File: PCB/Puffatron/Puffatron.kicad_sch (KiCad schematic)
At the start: 10 parts, among them U1 RP2040-ZERO, U10 ULN2803A, U2 MCP23017_SP, U3 ULN2803A, U4 MCP23017_SP, U5 MCP23017_SP, U6 ULN2803A, U7 ULN2803A, U8 ULN2803A, U9 ULN2803A

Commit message: README
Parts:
- added Brd1: SSD1306, symbol SSD1306-128x64_OLED:SSD1306
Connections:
- net GNDREF: now also Brd1.1 (GND)
- net at U1.10 (GP9): now also U1.4 (GP3), U1.5 (GP4), U1.6 (GP5), U1.7 (GP6), U1.8 (GP7), U1.9 (GP8), Brd1.3 (SCL)
- net at U1.23 (5V), U2.9 (VDD), U4.16 (A1)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: now also Brd1.2 (VCC)
- net at U1.3 (GP2): now also Brd1.4 (SDA)
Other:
- note added: "OLED"
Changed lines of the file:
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@@
     (date "2026-08-04")
   )
+  (junction (at 67.31 90.17) (diameter 0) (color 0 0 0 0)
+  )
   (junction (at 67.31 125.73) (diameter 0) (color 0 0 0 0)
   )
@@
   (junction (at 85.09 63.5) (diameter 0) (color 0 0 0 0)
   )
+  (junction (at 24.13 58.42) (diameter 0) (color 0 0 0 0)
+  )
   (junction (at 67.31 35.56) (diameter 0) (color 0 0 0 0)
   )
@@
   (junction (at 102.87 191.77) (diameter 0) (color 0 0 0 0)
   )
+  (junction (at 24.13 53.34) (diameter 0) (color 0 0 0 0)
+  )
   (junction (at 76.2 25.4) (diameter 0) (color 0 0 0 0)
   )
+  (junction (at 24.13 63.5) (diameter 0) (color 0 0 0 0)
+  )
   (junction (at 175.26 140.97) (diameter 0) (color 0 0 0 0)
   )
   (junction (at 175.26 82.55) (diameter 0) (color 0 0 0 0)
   )
+  (junction (at 24.13 66.04) (diameter 0) (color 0 0 0 0)
+  )
   (junction (at 175.26 99.06) (diameter 0) (color 0 0 0 0)
   )
   (junction (at 82.55 22.86) (diameter 0) (color 0 0 0 0)
   )
+  (junction (at 24.13 60.96) (diameter 0) (color 0 0 0 0)
+  )
+  (junction (at 24.13 55.88) (diameter 0) (color 0 0 0 0)
+  )
   (wire (pts (xy 125.73 60.96) (xy 129.54 60.96))
     (stroke (width 0) (type default))
@@
     (stroke (width 0) (type default))
   )
+  (wire (pts (xy 39.37 95.25) (xy 39.37 90.17))
+    (stroke (width 0) (type default))
+  )
+  (wire (pts (xy 24.13 86.36) (xy 41.91 86.36))
+    (stroke (width 0) (type default))
+  )
   (wire (pts (xy 125.73 115.57) (xy 125.73 123.19))
     (stroke (width 0) (type default))
@@
     (stroke (width 0) (type default))
   )
+  (wire (pts (xy 24.13 53.34) (xy 24.13 55.88))
+    (stroke (width 0) (type default))
+  )
   (wire (pts (xy 120.65 58.42) (xy 123.19 58.42))
     (stroke (width 0) (type default))
@@
     (stroke (width 0) (type default))
   )
+  (wire (pts (xy 24.13 58.42) (xy 24.13 60.96))
+    (stroke (width 0) (type default))
+  )
   (wire (pts (xy 24.13 16.51) (xy 82.55 16.51))
     (stroke (width 0) (type default))
   )
+  (wire (pts (xy 44.45 81.28) (xy 44.45 95.25))
+    (stroke (width 0) (type default))
+  )
   (wire (pts (xy 168.91 140.97) (xy 175.26 140.97))
     (stroke (width 0) (type default))
@@
     (stroke (width 0) (type default))
   )
+  (wire (pts (xy 24.13 66.04) (xy 24.13 86.36))
+    (stroke (width 0) (type default))
+  )
   (wire (pts (xy 120.65 113.03) (xy 127 113.03))
     (stroke (width 0) (type default))
@@
     (stroke (width 0) (type default))
   )
+  (wire (pts (xy 41.91 86.36) (xy 41.91 95.25))
+    (stroke (width 0) (type default))
+  )
+  (wire (pts (xy 24.13 55.88) (xy 24.13 58.42))
+    (stroke (width 0) (type default))
+  )
   (wire (pts (xy 128.27 118.11) (xy 129.54 118.11))
     (stroke (width 0) (type default))
@@
     (stroke (width 0) (type default))
   )
+  (wire (pts (xy 24.13 60.96) (xy 24.13 63.5))
+    (stroke (width 0) (type default))
+  )
   (wire (pts (xy 128.27 175.26) (xy 129.54 175.26))
     (stroke (width 0) (type default))
@@
     (stroke (width 0) (type default))
   )
+  (wire (pts (xy 19.05 81.28) (xy 44.45 81.28))
+    (stroke (width 0) (type default))
+  )
   (wire (pts (xy 127 58.42) (xy 129.54 58.42))
     (stroke (width 0) (type default))
   )
+  (wire (pts (xy 36.83 95.25) (xy 22.86 95.25))
+    (stroke (width 0) (type default))
+  )
   (wire (pts (xy 120.65 40.64) (xy 148.59 40.64))
     (stroke (width 0) (type default))
   )
+  (wire (pts (xy 22.86 95.25) (xy 22.86 99.06))
+    (stroke (width 0) (type default))
+  )
+  (wire (pts (xy 24.13 63.5) (xy 24.13 66.04))
+    (stroke (width 0) (type default))
+  )
+  (wire (pts (xy 24.13 48.26) (xy 19.05 48.26))
+    (stroke (width 0) (type default))
+  )
+  (wire (pts (xy 67.31 90.17) (xy 67.31 125.73))
+    (stroke (width 0) (type default))
+  )
   (wire (pts (xy 148.59 161.29) (xy 120.65 161.29))
     (stroke (width 0) (type default))
@@
     (stroke (width 0) (type default))
   )
+  (wire (pts (xy 24.13 50.8) (xy 24.13 53.34))
+    (stroke (width 0) (type default))
+  )
   (wire (pts (xy 127 50.8) (xy 127 58.42))
     (stroke (width 0) (type default))
@@
     (stroke (width 0) (type default))
   )
+  (wire (pts (xy 39.37 90.17) (xy 67.31 90.17))
+    (stroke (width 0) (type default))
+  )
   (wire (pts (xy 120.65 184.15) (xy 120.65 190.5))
     (stroke (width 0) (type default))
@@
     (stroke (width 0) (type default))
   )
+  (wire (pts (xy 19.05 48.26) (xy 19.05 81.28))
+    (stroke (width 0) (type default))
+  )
   (wire (pts (xy 125.73 180.34) (xy 129.54 180.34))
     (stroke (width 0) (type default))
@@
     (stroke (width 0) (type default))
   )
-  (wire (pts (xy 67.31 77.47) (xy 67.31 125.73))
+  (wire (pts (xy 67.31 77.47) (xy 67.31 90.17))
     (stroke (width 0) (type default))
   )
@@
   )
   (text "PSU" (at 185.42 92.71 0)
+    (effects (font (size 1.27 1.27)) (justify left bottom))
+  )
+  (text "OLED" (at 38.1 106.68 0)
     (effects (font (size 1.27 1.27)) (justify left bottom))
   )
@@
     )
   )
+  (symbol (lib_id "power:GNDREF") (at 22.86 99.06 0) (unit 1)
+    (in_bom yes) (on_board yes) (dnp no) (fields_autoplaced)
+    (property "Reference" "#PWR010" (at 22.86 105.41 0)
+      (effects (font (size 1.27 1.27)) hide)
+    )
+    (property "Value" "GNDREF" (at 22.86 104.14 0)
+      (effects (font (size 1.27 1.27)))
+    )
+    (property "Footprint" "" (at 22.86 99.06 0)
+      (effects (font (size 1.27 1.27)) hide)
+    )
+    (property "Datasheet" "" (at 22.86 99.06 0)
+      (effects (font (size 1.27 1.27)) hide)
+    )
+    (pin "1")
+    (instances
+      (project "Puffatron"
+        (path "/96bd69bf-07b6-413b-a4db-7565e08c99f5"
+          (reference "#PWR010") (unit 1)
+        )
+      )
+    )
+  )
   (symbol (lib_id "power:GNDREF") (at 59.69 71.12 0) (unit 1)
     (in_bom yes) (on_board yes) (dnp no) (fields_autoplaced)
@@
         )
       )
+    )
+  )
+  (symbol (lib_id "SSD1306-128x64_OLED:SSD1306") (at 40.64 104.14 0) (unit 1)
+    (in_bom yes) (on_board yes) (dnp no) (fields_autoplaced)
+    (property "Reference" "Brd1" (at 48.26 102.87 0)
+      (effects (font (size 1.27 1.27)) (justify left))
+    )
+    (property "Value" "SSD1306" (at 48.26 105.41 0)
+      (effects (font (size 1.27 1.27)) (justify left))
+    )
+    (property "Footprint" "" (at 40.64 97.79 0)
+      (effects (font (size 1.27 1.27)) hide)
+    )
+    (property "Datasheet" "" (at 40.64 97.79 0)
+      (effects (font (size 1.27 1.27)) hide)
+    )
+    (pin "3")
+    (pin "4")
+    (pin "1")
+    (pin "2")
+    (instances
+      (project "Puffatron"
+        (path "/96bd69bf-07b6-413b-a4db-7565e08c99f5"
+          (reference "Brd1") (unit 1)
+        )
+      )

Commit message: Reorg code, update schematic and README
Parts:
- added R1, R2: R_Small, symbol Device:R_Small
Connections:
- net at Brd1.2 (VCC), U2.9 (VDD), U4.16 (A1)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: now also U1.21 (3V3), U2.18 (~{RESET}), U4.18 (~{RESET}), U5.18 (~{RESET}), R1.1, R2.1; no longer U1.23 (5V)
- net at U1.1 (GP0), U2.13 (SDA), U5.13 (SDA): now also U4.13 (SDA), R2.2
- net at U1.2 (GP1), U2.12 (SCK), U5.12 (SCK): now also U4.12 (SCK), R1.2
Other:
- note added: "4k7"

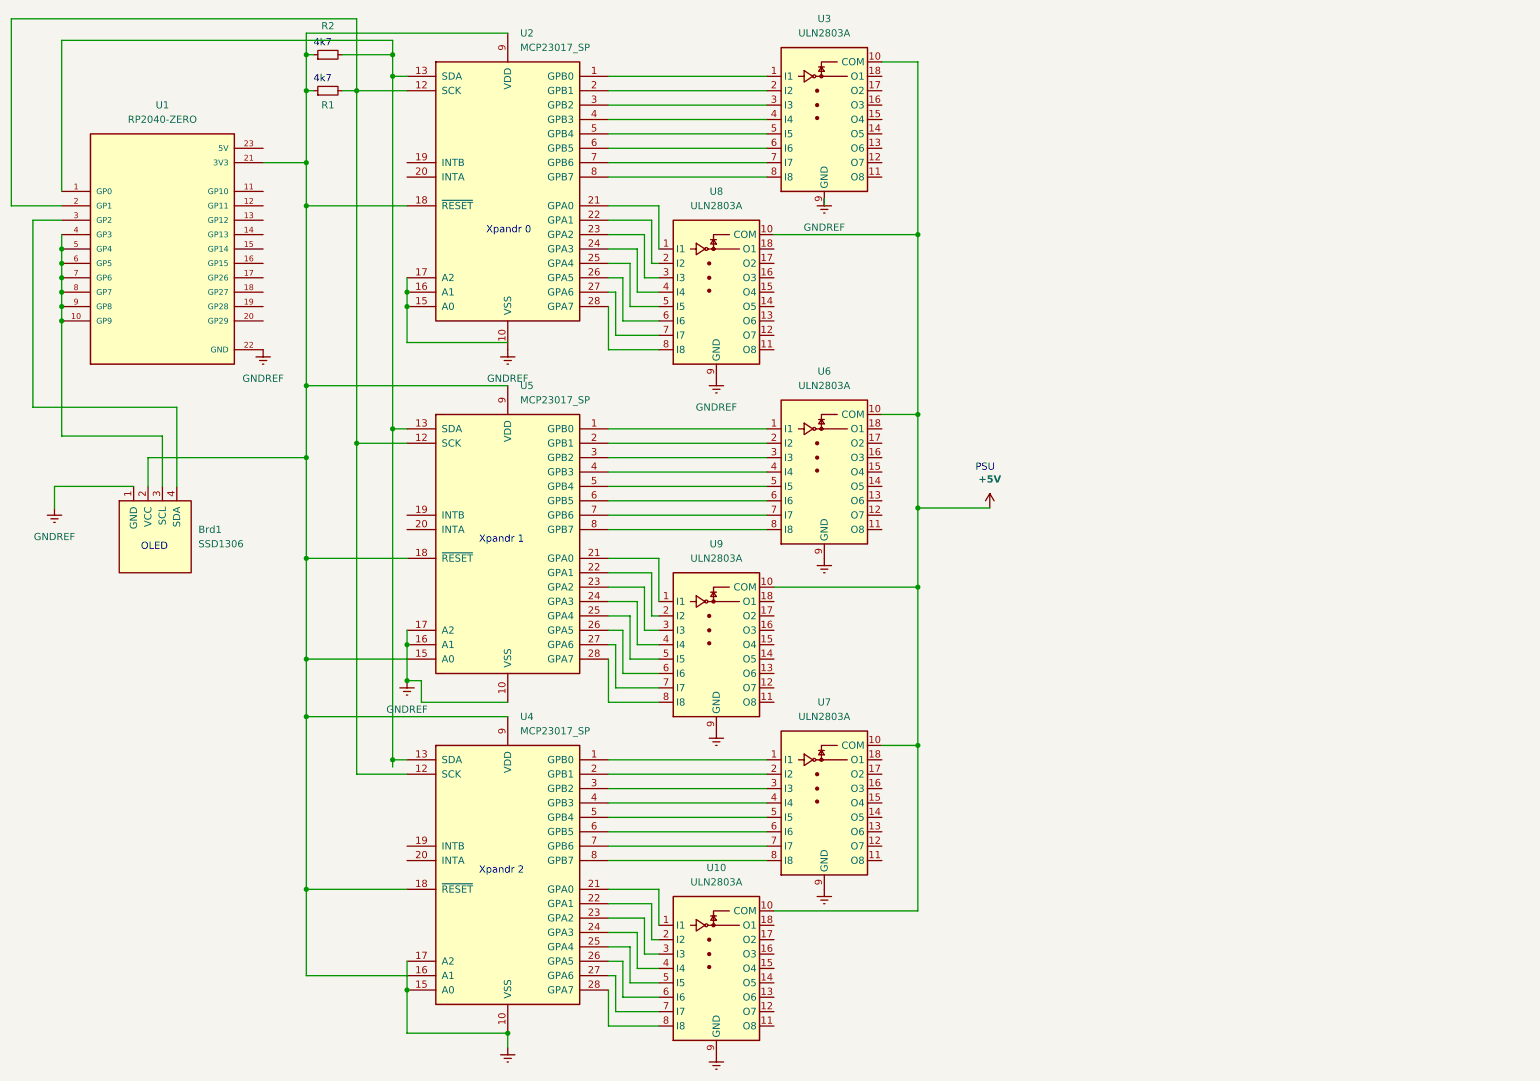
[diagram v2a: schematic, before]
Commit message: Add I2C constants, correct schematic, uptdate docs
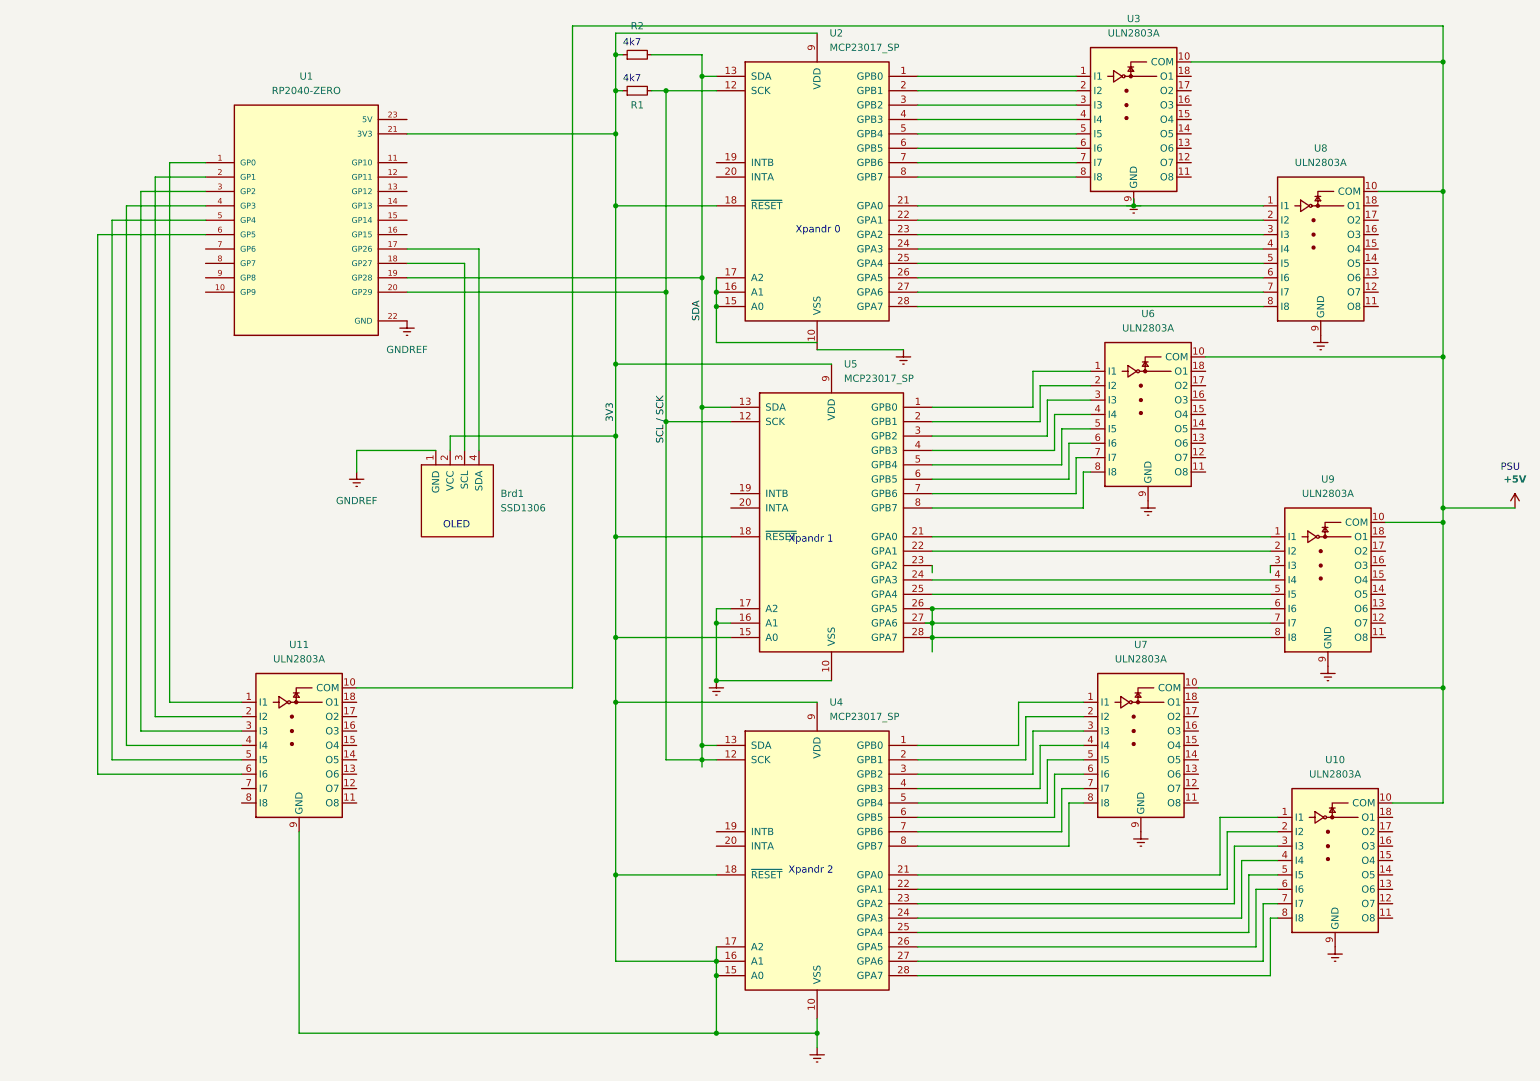
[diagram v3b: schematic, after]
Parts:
- added U11: ULN2803A, symbol Transistor_Array:ULN2803A
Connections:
- net +5V: now also U11.10 (COM)
- net GNDREF: now also Brd1.2 (VCC), R1.1, R2.1, U1.21 (3V3), U2.18 (~{RESET}), U2.21 (GPA0), U2.9 (VDD), U4.16 (A1), U4.18 (~{RESET}), U4.9 (VDD), U5.15 (A0), U5.18 (~{RESET}), U5.9 (VDD), U8.1 (I1), U11.9 (GND)
- net SCL / SCK: now reaches R1.2, U2.12 (SCK), U4.12 (SCK), U5.12 (SCK)
- net SCL / SCK: now also R2.2, U1.19 (GP28), U1.20 (GP29), U2.13 (SDA), U4.13 (SDA), U5.13 (SDA); no longer U1.2 (GP1)
- net at Brd1.4 (SDA): now also U1.17 (GP26); no longer U1.3 (GP2)
- net at U1.18 (GP27): now also Brd1.3 (SCL)
- net at U9.3 (I3): no longer U5.23 (GPA2)
- net at U5.26 (GPA5), U9.6 (I6): now also U5.27 (GPA6), U5.28 (GPA7), U9.7 (I7), U9.8 (I8)
- new net: U1.1 (GP0), U11.1 (I1)
- new net: U1.2 (GP1), U11.2 (I2)
- new net: U1.3 (GP2), U11.3 (I3)
- new net: U1.4 (GP3), U11.4 (I4)
- new net: U1.5 (GP4), U11.5 (I5)
- new net: U1.6 (GP5), U11.6 (I6)
- now unconnected: U1.10 (GP9), U1.7 (GP6), U1.8 (GP7), U1.9 (GP8)
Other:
- moved on the sheet: Brd1, R1, R2, U1, U10, U2, U3, U4, U5, U6, U7, U8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
